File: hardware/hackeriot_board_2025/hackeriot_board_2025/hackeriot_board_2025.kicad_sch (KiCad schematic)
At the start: 105 parts, among them J1 USB_B_Micro, J2 Conn_01x02_Socket, J3 Conn_01x03_Socket, J4 Conn_01x03_Socket, J5 Conn_01x05_Socket, J6 DebugEdge_02x05, SW1 SW_Push, SW2 SW_Push, SW3 SW_Push, SW4 SW_Push, SW5 SW_Push, SW6 SW_Push, SW7 SW_Push, U1 STM32G030F6Px, U2 HT16K33A-28SOP, U3 AP2112K-3.3, U4 PCA9306DCUR, U5 LIS3DH

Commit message: Add MPN for all components
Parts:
- removed J2: Conn_01x02_Socket, symbol Connector:Conn_01x02_Socket
- C1: value 100nf -> 100 nF
- C2, C3: footprint (none) -> Capacitor_SMD:C_0805_2012Metric_Pad1.18x1.45mm_HandSolder
- C4: value 100nF -> 100 nF; footprint (none) -> Capacitor_SMD:C_0805_2012Metric_Pad1.18x1.45mm_HandSolder; MPN (none) -> C49678
- C5: footprint (none) -> Capacitor_SMD:C_0805_2012Metric_Pad1.18x1.45mm_HandSolder; MPN (none) -> C15850
- C6: footprint (none) -> Capacitor_SMD:C_0805_2012Metric_Pad1.18x1.45mm_HandSolder; MPN (none) -> C49678
- C7: footprint (none) -> Capacitor_SMD:C_0805_2012Metric_Pad1.18x1.45mm_HandSolder; MPN (none) -> C1779
- D65, D66: footprint (none) -> LED_SMD:LED_0805_2012Metric_Pad1.15x1.40mm_HandSolder
- J1: footprint (none) -> Connector_USB:USB_Micro-B_Amphenol_10103594-0001LF_Horizontal; MPN (none) -> C428495
- J3, J4: MPN (none) -> C146243
- J5: MPN (none) -> C50950
- R10, R11, R2, R6, R7, R8, R9: footprint (none) -> Resistor_SMD:R_0805_2012Metric_Pad1.20x1.40mm_HandSolder
- R3: footprint (none) -> Resistor_SMD:R_0805_2012Metric_Pad1.20x1.40mm_HandSolder; MPN (none) -> C17734
- R4: footprint (none) -> Resistor_SMD:R_0805_2012Metric_Pad1.20x1.40mm_HandSolder; MPN (none) -> C17513
- R5: value 100K -> 200K; footprint (none) -> Resistor_SMD:R_0805_2012Metric_Pad1.20x1.40mm_HandSolder; MPN (none) -> C17539
- SW1, SW2, SW3, SW4, SW5, SW6, SW7: MPN C22375334 -> C22375341
- TP1, TP2, TP3: footprint (none) -> TestPoint:TestPoint_Pad_D2.0mm
- U1: footprint (none) -> Package_SO:TSSOP-20_4.4x6.5mm_P0.65mm
- U5: MPN (none) -> C15134
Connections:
- net VBUS: no longer U4.7 (VREF2)
- net at R5.1, U4.8 (EN): now also U4.7 (VREF2)
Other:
- moved on the sheet: R5

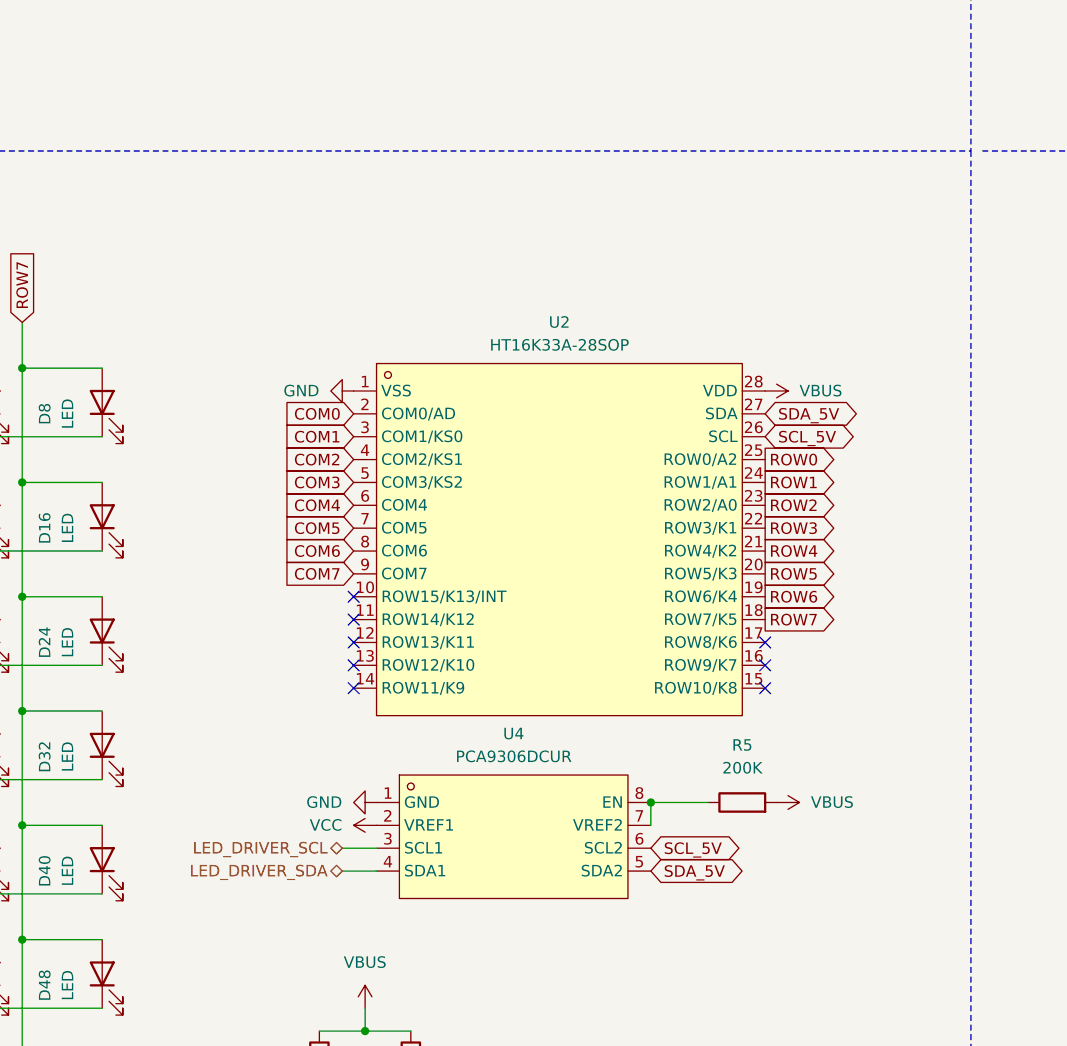
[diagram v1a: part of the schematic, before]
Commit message: Add missing footprint and update MPN
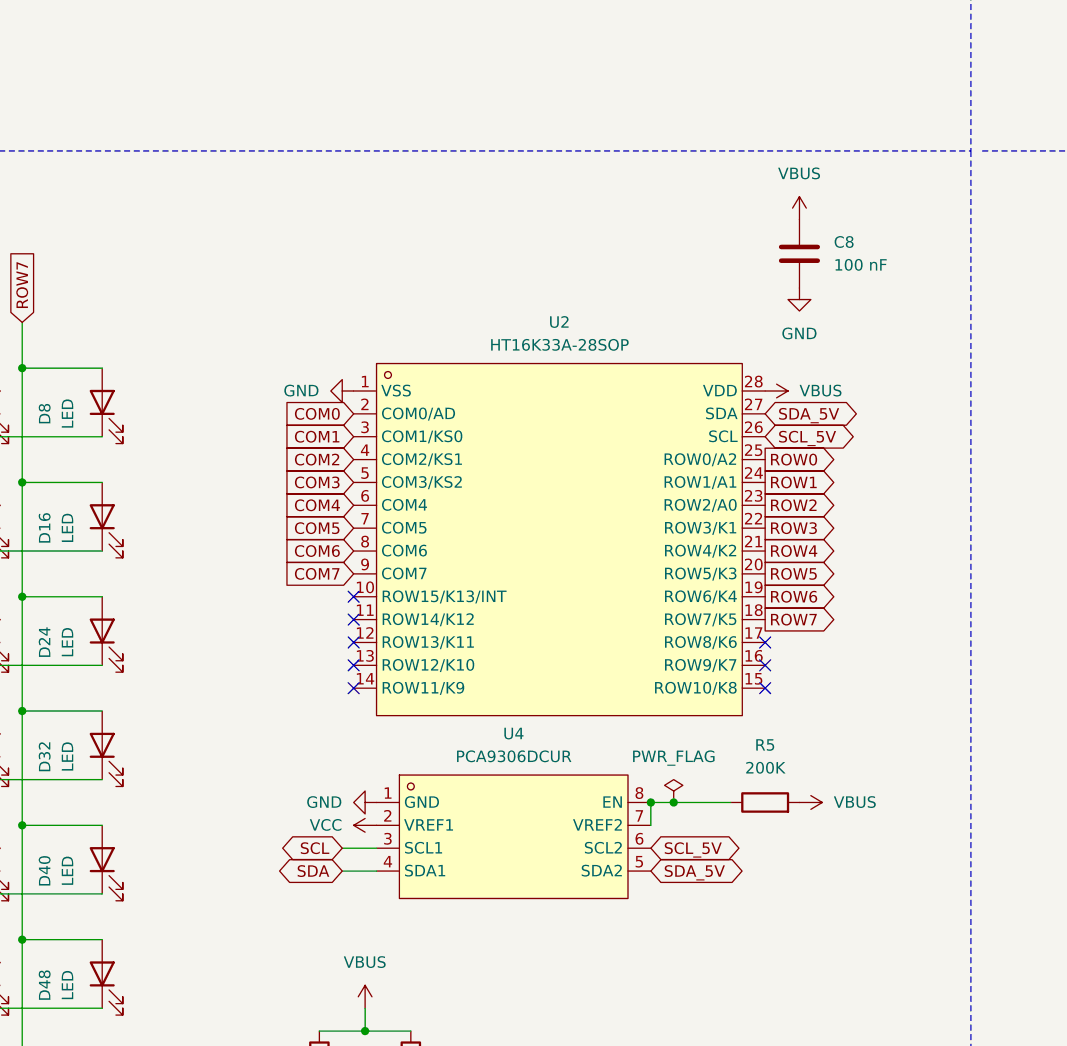
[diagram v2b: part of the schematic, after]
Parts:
- added C8: 100 nF, Capacitor_SMD:C_0805_2012Metric_Pad1.18x1.45mm_HandSolder, symbol Device:C
- J3, J4: footprint (none) -> Connector_PinSocket_2.54mm:PinSocket_1x03_P2.54mm_Vertical
- J5: footprint (none) -> Connector_PinSocket_2.54mm:PinSocket_1x05_P2.54mm_Vertical
- J6: footprint hackeriot_2025:DebugEdge_2x05_Target -> hackeriot_board_2025:DebugEdge_2x05_Target
- SW1, SW2, SW3, SW4, SW5, SW6, SW7: footprint (none) -> hackeriot_board_2025:SW-SMD_4P-L6.0-W6.0-P4.50-LS9.0-2
- U2: footprint hackeriot_2025:SOP-28_L17.9-W7.5-P1.27-LS10.3-BL -> hackeriot_board_2025:SOP-28_L17.9-W7.5-P1.27-LS10.3-BL
- U4: footprint hackeriot_2025:SSOP-8_L2.0-W2.3-P0.50-LS3.1-BR -> hackeriot_board_2025:SSOP-8_L2.0-W2.3-P0.50-LS3.1-BR
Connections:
- net LED_DRIVER_SCL is gone; now on net SCL: U4.3 (SCL1)
- net LED_DRIVER_SDA is gone; now on net SDA: U4.4 (SDA1)
- net GND: now also C8.2
- net VBUS: now also C8.1
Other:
- moved on the sheet: R5

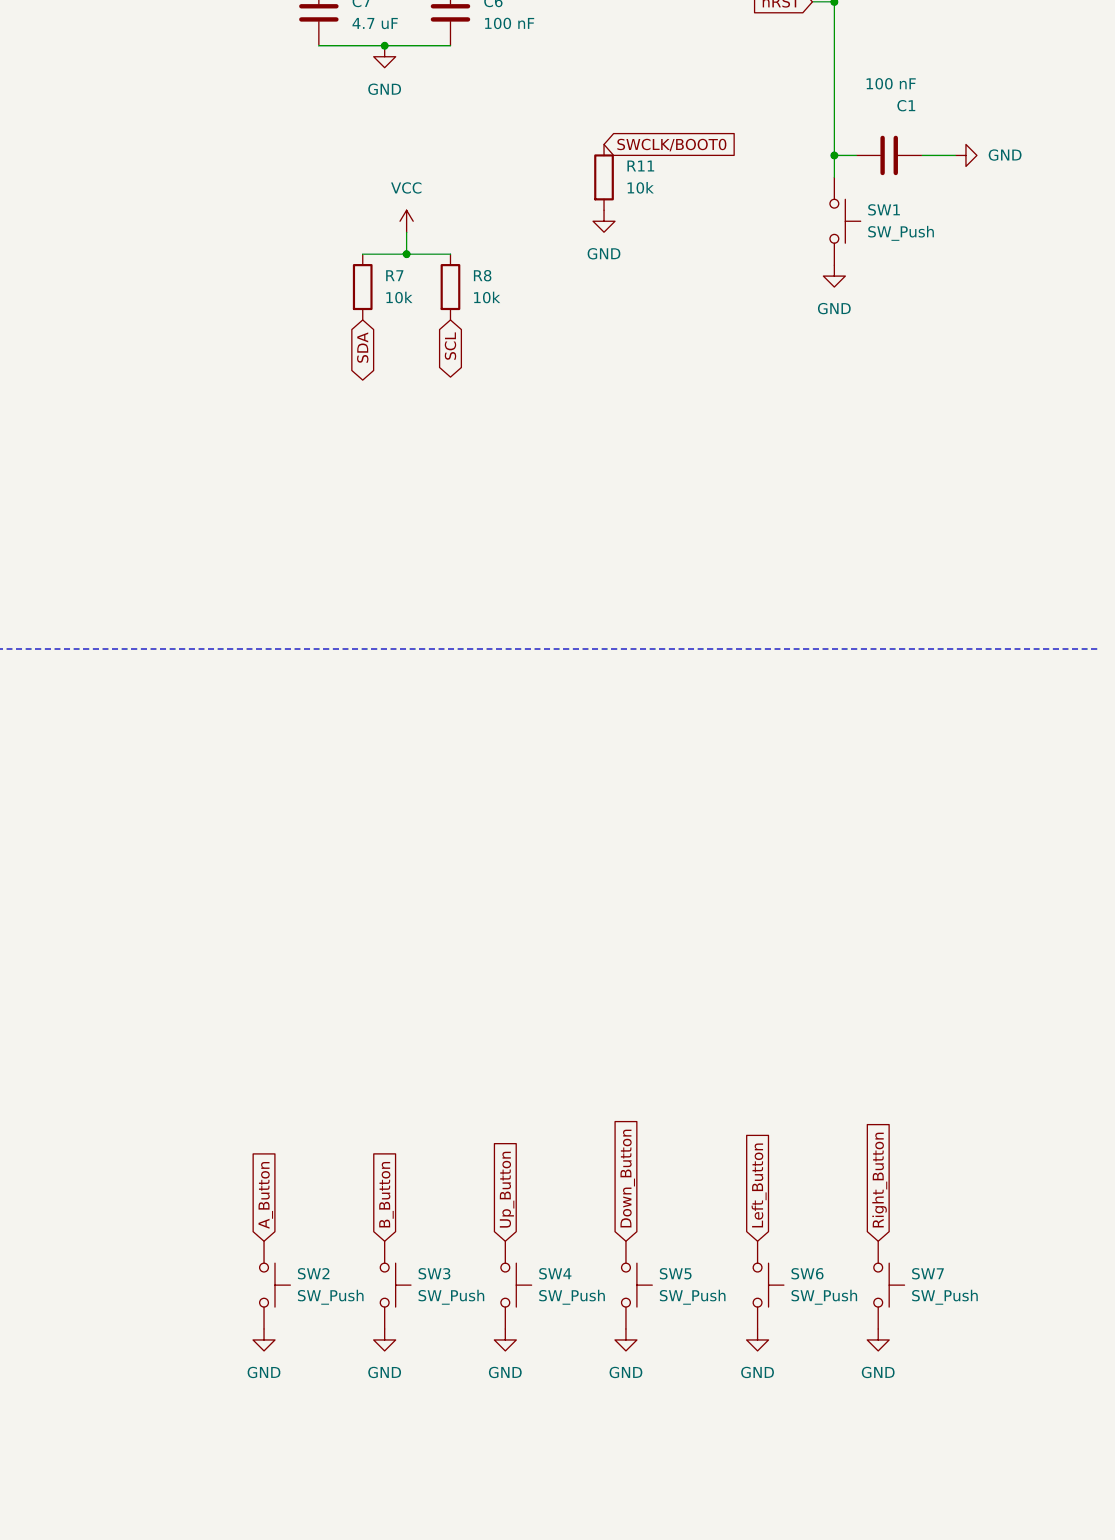
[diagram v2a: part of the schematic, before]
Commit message: Fix symbols and footprints
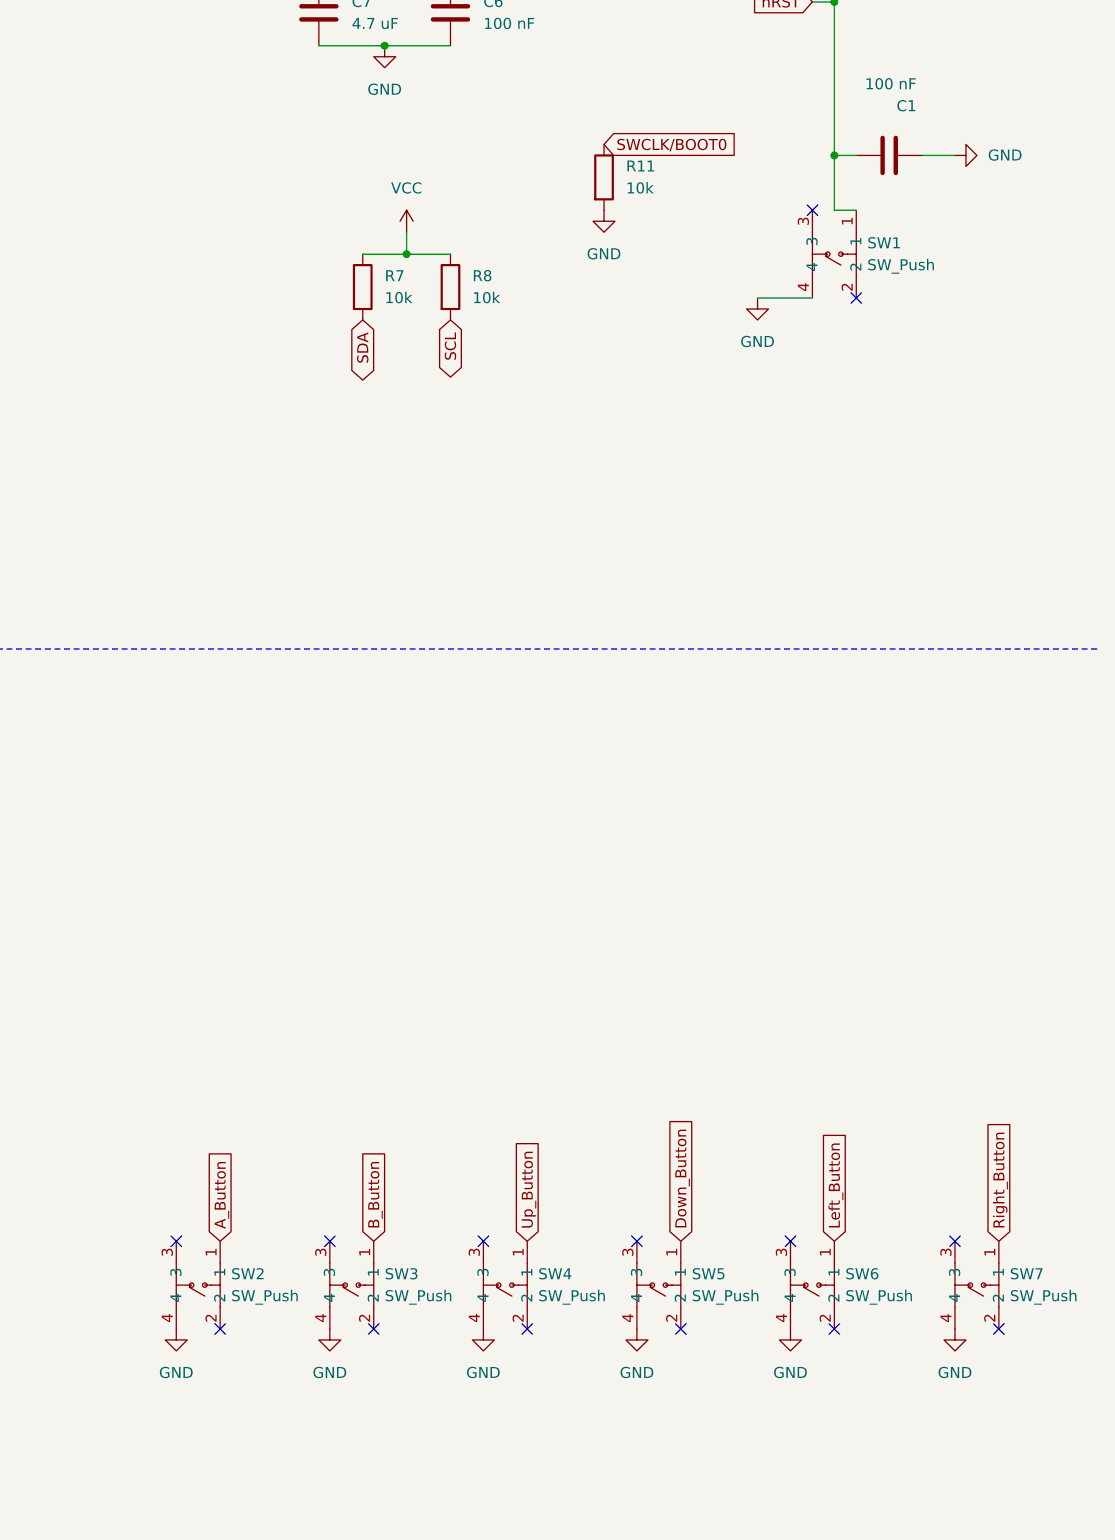
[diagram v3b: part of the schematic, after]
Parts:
- J6: symbol hackeriot_2025:DebugEdge_02x05 -> hackeriot_board_2025:DebugEdge_02x05
- SW1, SW2, SW3, SW4, SW5, SW6, SW7: symbol Switch:SW_Push -> hackeriot_board_2025:TS110426045; LCSC Part (none) -> C22375341
- U4: symbol hackeriot_2025:PCA9306DCUR -> hackeriot_board_2025:PCA9306DCUR
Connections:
- net GND: now also SW1.4, SW2.4, SW3.4, SW4.4, SW5.4, SW6.4, SW7.4; no longer SW1.2, SW2.2, SW3.2, SW4.2, SW5.2, SW6.2, SW7.2
- no-connect marks 22 -> 36

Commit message: Update schematic and symbol library
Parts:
- removed C4: 100 nF, Capacitor_SMD:C_0805_2012Metric_Pad1.18x1.45mm_HandSolder, symbol Device:C
- removed C5: 10 uF, Capacitor_SMD:C_0805_2012Metric_Pad1.18x1.45mm_HandSolder, symbol Device:C
- removed R6: 10K, Resistor_SMD:R_0805_2012Metric_Pad1.20x1.40mm_HandSolder, symbol Device:R
- removed U1: STM32G030F6Px, Package_SO:TSSOP-20_4.4x6.5mm_P0.65mm, symbol MCU_ST_STM32G0:STM32G030F6Px
- removed U5: LIS3DH, Package_LGA:LGA-16_3x3mm_P0.5mm_LayoutBorder3x5y, symbol Sensor_Motion:LIS3DH
- added J2: Conn_02x08_Odd_Even, Connector_PinSocket_2.54mm:PinSocket_2x08_P2.54mm_Vertical, symbol Connector_Generic:Conn_02x08_Odd_Even
- added U1: STM32G030C8Tx, Package_QFP:LQFP-48_7x7mm_P0.5mm, symbol MCU_ST_STM32G0:STM32G030C8Tx
- added U5: AT24C256C-SSHL-T, hackeriot_board_2025:SOIC-8_L4.9-W3.9-P1.27-LS6.0-BL, symbol hackeriot_board_2025:AT24C256C-SSHL-T
- D1, D10, D11, D12, D13, D14, D15, D16, D17, D18, D19, D2, D20, D21, D22, D23, D24, D25, D26, D27, D28, D29, D3, D30, D31, D32, D33, D34, D35, D36, D37, D38, D39, D4, D40, D41, D42, D43, D44, D45, D46, D47, D48, D49, D5, D50, D51, D52, D53, D54, D55, D56, D57, D58, D59, D6, D60, D61, D62, D63, D64, D7, D8, D9: MPN (none) -> C84256
- U2: symbol EasyEDA:HT16K33A-28SOP -> hackeriot_board_2025:HT16K33A-28SOP
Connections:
- net A_Button: now also U1.11 (PA0)
- net B_Button: now also U1.12 (PA1)
- net DEBUG_UART_RX: now also U1.14 (PA3)
- net DEBUG_UART_TX: now also U1.13 (PA2)
- net Down_Button: now also U1.16 (PA5)
- net GND: now also U1.5 (VREF+), U1.7 (VSS), U5.1 (A0), U5.2 (A1), U5.3 (A2), U5.4 (GND), U5.7 (WP)
- net Left_Button: now also U1.17 (PA6)
- net Right_Button: now also U1.18 (PA7)
- net SCL: now also U1.33 (PA9/PA11), U5.6 (SCL)
- net SDA: now also U1.34 (PA10/PA12), U5.5 (SDA)
- net SWCLK/BOOT0: now also U1.36 (PA14)
- net SWDIO: now also U1.35 (PA13)
- net Up_Button: now also U1.15 (PA4)
- net VCC: now also U1.4 (VBAT), U1.6 (VDD), U5.8 (VCC)
- net nRST: now also U1.10 (NRST)
- new net PB0: J2.1 (Pin_1), U1.19 (PB0)
- new net PB1: J2.3 (Pin_3), U1.20 (PB1)
- new net PB10: J2.6 (Pin_6), U1.22 (PB10)
- new net PB11: J2.8 (Pin_8), U1.23 (PB11)
- new net PB12: J2.10 (Pin_10), U1.24 (PB12)
- new net PB13: J2.12 (Pin_12), U1.25 (PB13)
- new net PB14: J2.14 (Pin_14), U1.26 (PB14)
- new net PB15: J2.16 (Pin_16), U1.27 (PB15)
- new net PB2: J2.5 (Pin_5), U1.21 (PB2)
- new net PB3: J2.7 (Pin_7), U1.42 (PB3)
- new net PB4: J2.9 (Pin_9), U1.43 (PB4)
- new net PB5: J2.11 (Pin_11), U1.44 (PB5)
- new net PB6: J2.13 (Pin_13), U1.45 (PB6)
- new net PB7: J2.15 (Pin_15), U1.46 (PB7)
- new net PB8: J2.2 (Pin_2), U1.47 (PB8)
- new net PB9: J2.4 (Pin_4), U1.48 (PB9)
- no-connect marks 36 -> 42
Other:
- note removed: "Accelerometer"
- moved on the sheet: C1, C6, C7, R1, R11, R7, R8, SW1

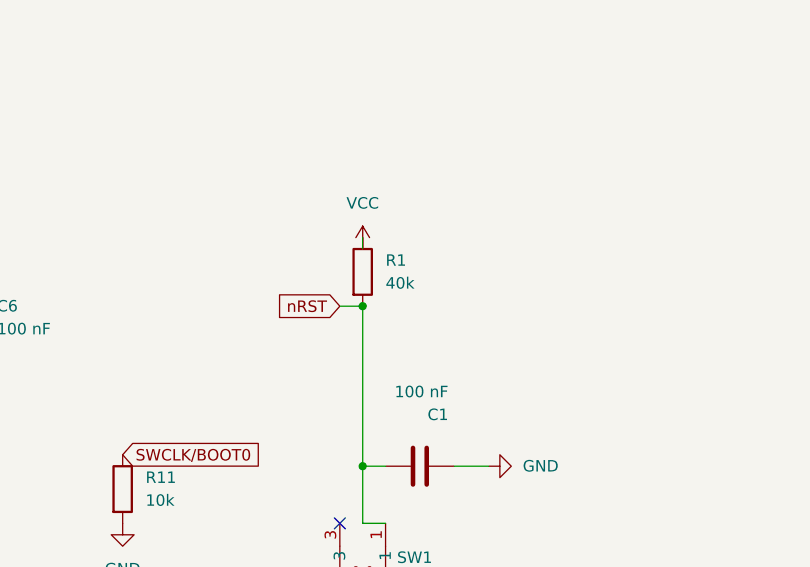
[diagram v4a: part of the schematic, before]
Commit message: Update layout and component ids
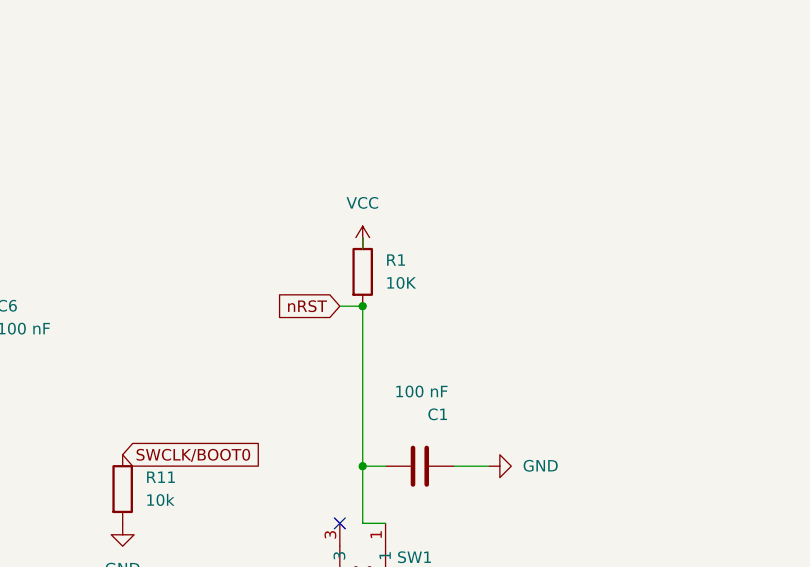
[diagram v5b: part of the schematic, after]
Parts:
- C1, C6, C8: LCSC (none) -> C49678; MPN C49678 -> (none)
- C2, C3: LCSC (none) -> C28323; MPN C28323 -> (none)
- C7: LCSC (none) -> C1779; MPN C1779 -> (none)
- D1, D10, D11, D12, D13, D14, D15, D16, D17, D18, D19, D2, D20, D21, D22, D23, D24, D25, D26, D27, D28, D29, D3, D30, D31, D32, D33, D34, D35, D36, D37, D38, D39, D4, D40, D41, D42, D43, D44, D45, D46, D47, D48, D49, D5, D50, D51, D52, D53, D54, D55, D56, D57, D58, D59, D6, D60, D61, D62, D63, D64, D7, D8, D9: LCSC (none) -> C84256; MPN C84256 -> (none)
- D65: LCSC (none) -> C2297; MPN C2297 -> (none)
- D66: LCSC (none) -> C2296; MPN C2296 -> (none)
- J1: LCSC (none) -> C428495; MPN C428495 -> (none)
- J3, J4: LCSC (none) -> C146243; MPN C146243 -> (none)
- J5: LCSC (none) -> C50950; MPN C50950 -> (none)
- R1: value 40k -> 10K; LCSC (none) -> C17414; MPN C17633 -> (none)
- R10, R11, R2, R7, R8, R9: LCSC (none) -> C17414; MPN C17414 -> (none)
- R3: LCSC (none) -> C17734; MPN C17734 -> (none)
- R4: LCSC (none) -> C17513; MPN C17513 -> (none)
- R5: LCSC (none) -> C17539; MPN C17539 -> (none)
- SW1, SW2, SW3, SW4, SW5, SW6, SW7: LCSC (none) -> C22375341; MPN C22375341 -> (none)
- U1: LCSC (none) -> C529329; MPN C529329 -> (none)
- U2: LCSC (none) -> C5444737; MPN C5444737 -> (none)
- U3: LCSC (none) -> C51118; MPN C51118 -> (none)
- U4: LCSC (none) -> C33196; MPN C33196 -> (none)
- U5: LCSC (none) -> C6482; MPN C6482 -> (none)

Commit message: Fix rotations
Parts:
- J3, J4: LCSC Part (none) -> C146243
- J5: LCSC Part (none) -> C50950
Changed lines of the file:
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@@
 			)
 		)
+		(property "LCSC Part" " C146243"
+			(at 165.1 92.71 0)
+			(effects
+				(font
+					(size 1.27 1.27)
+				)
+				(hide yes)
+			)
+		)
 		(pin "1"
 		)
@@
 			)
 		)
+		(property "LCSC Part" " C146243"
+			(at 165.1 102.87 0)
+			(effects
+				(font
+					(size 1.27 1.27)
+				)
+				(hide yes)
+			)
+		)
 		(pin "3"
 		)
@@
 			(at 165.1 115.57 0)
 			(effects
+				(font
+					(size 1.27 1.27)
+				)
+				(hide yes)
+			)
+		)
+		(property "LCSC Part" " C50950"
+			(at 165.1 115.57 0)
+			(effects
